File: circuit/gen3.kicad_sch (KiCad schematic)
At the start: 5 parts, among them J1 Conn_01x02_Socket, J2 Conn_02x20_Row_Letter_Last, J3 Conn_01x02_Socket, J4 Conn_02x20_Row_Letter_Last, U1 ESP32-DevKitC

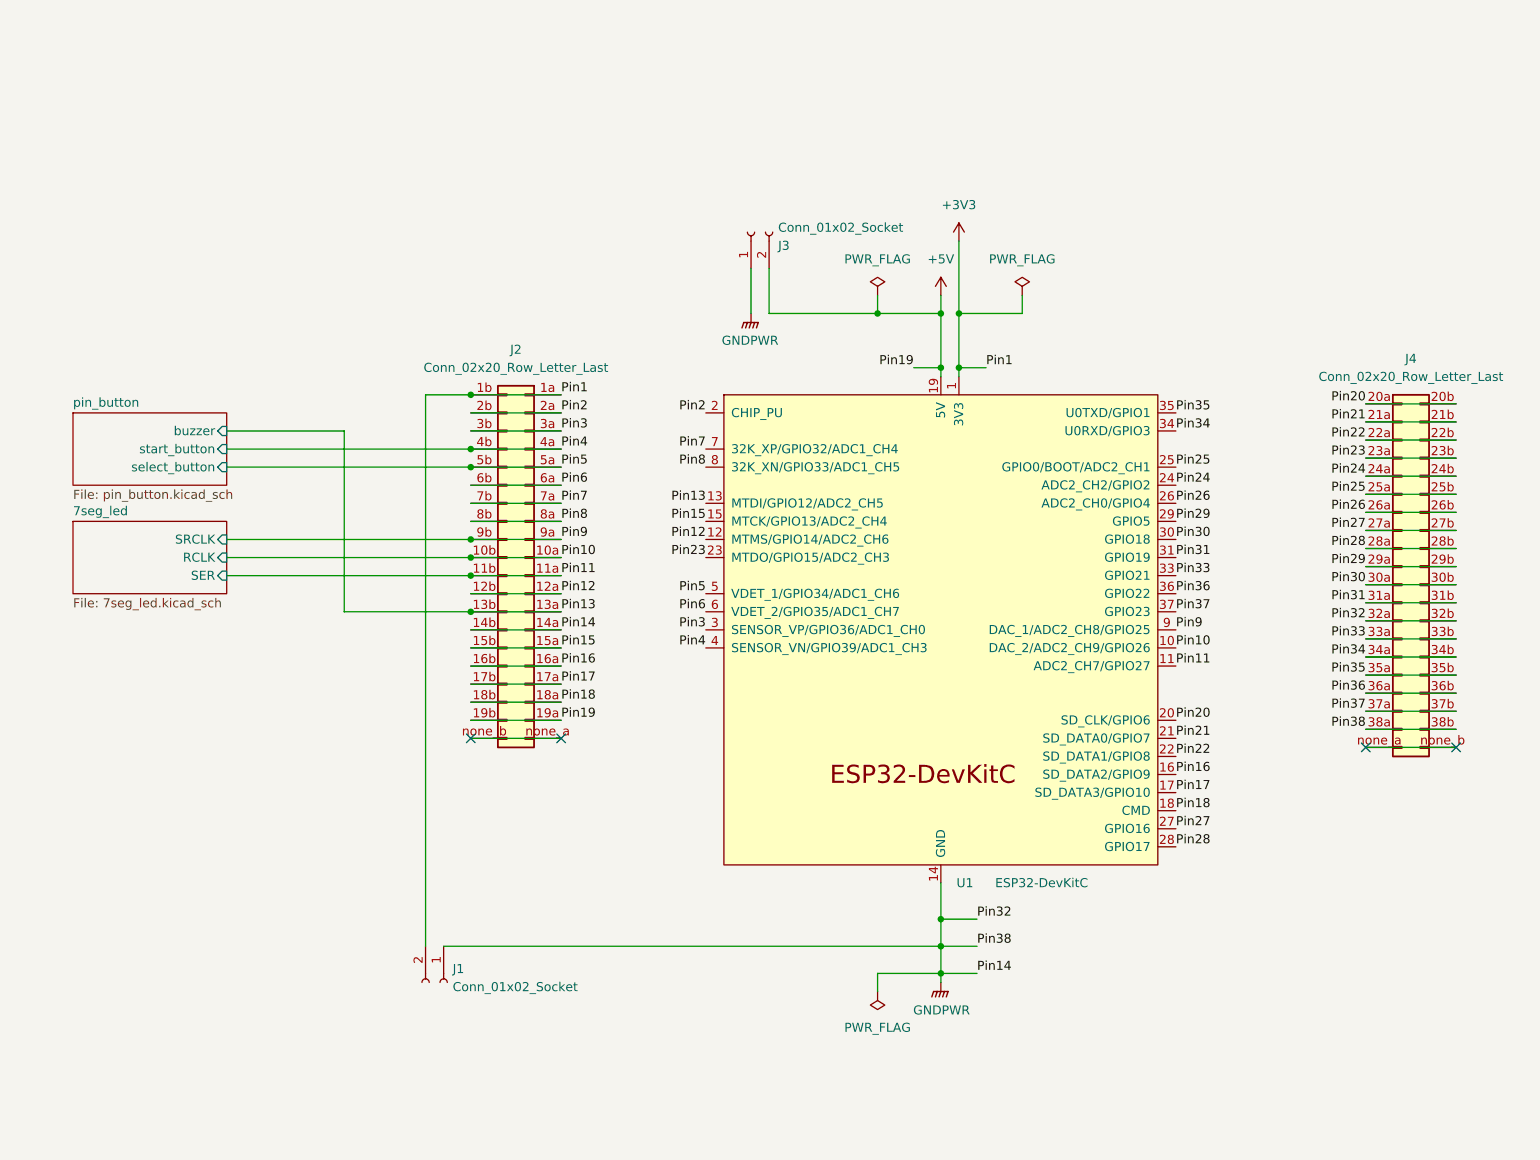
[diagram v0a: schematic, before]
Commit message: [add] add DC jack
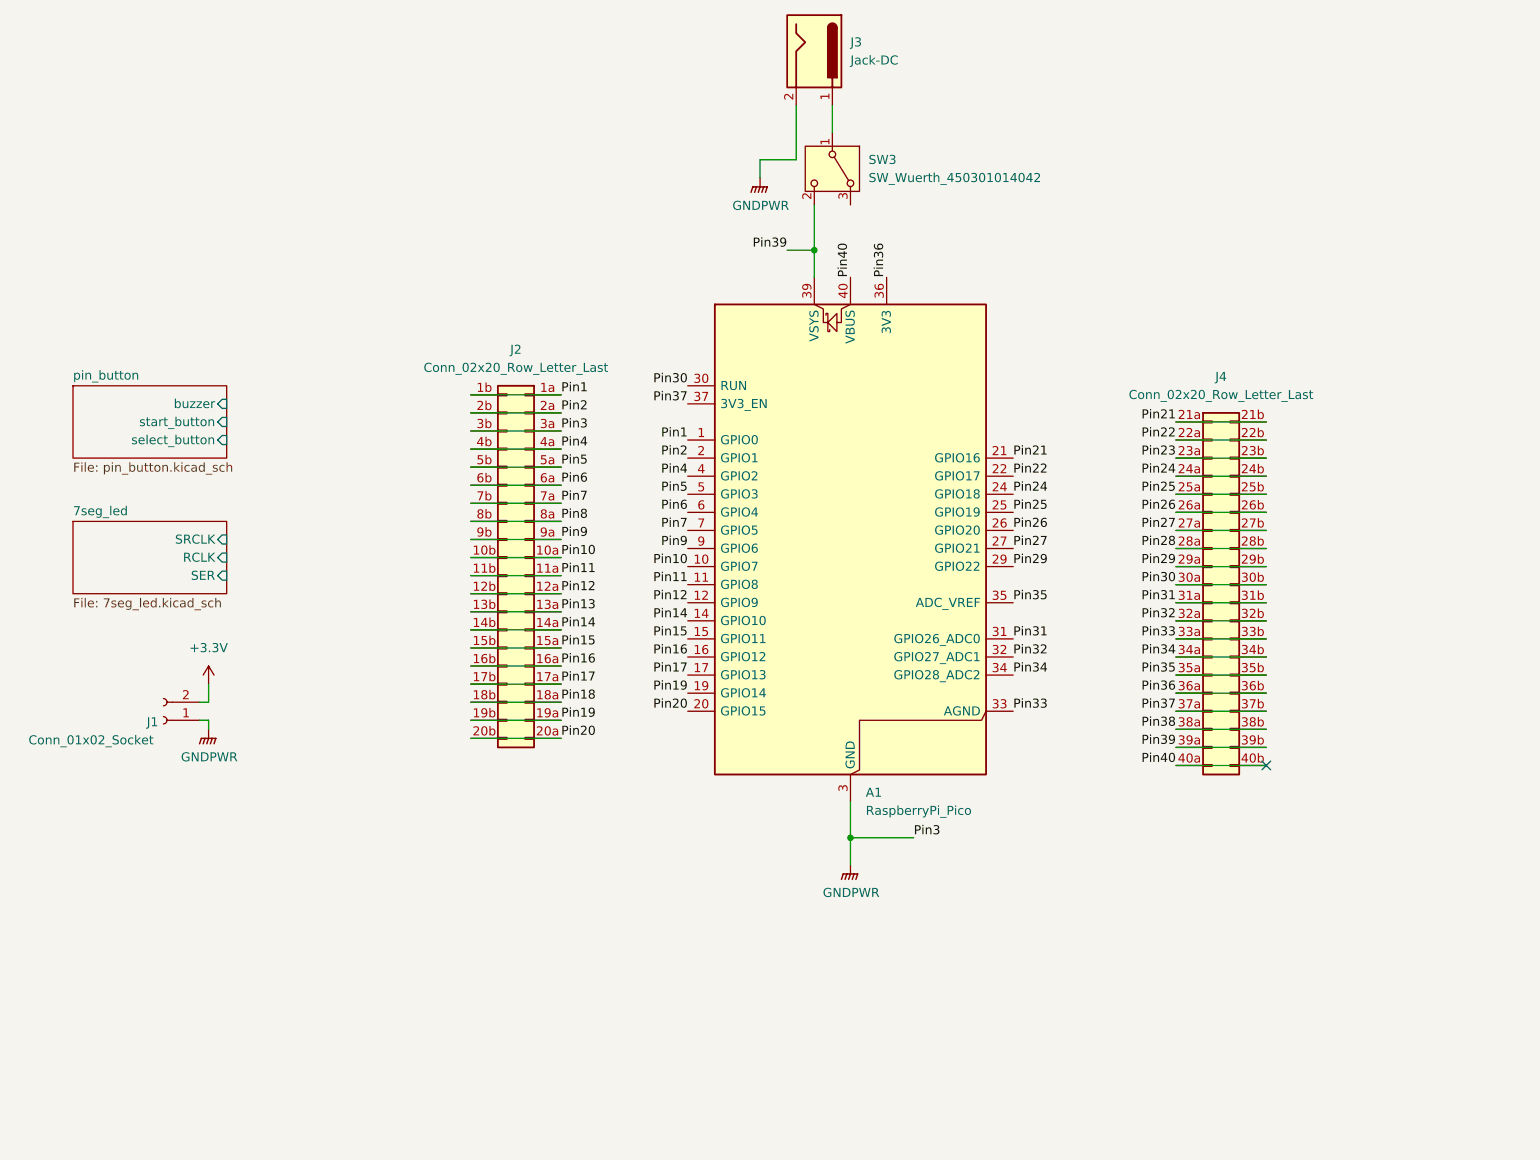
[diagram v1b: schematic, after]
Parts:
- removed J3: Conn_01x02_Socket, Connector_JST:JST_XH_S2B-XH-A_1x02_P2.50mm_Horizontal, symbol Connector:Conn_01x02_Socket
- removed U1: ESP32-DevKitC, MyPartsLibrary:ESP32-DevKitC, symbol PCM_Espressif:ESP32-DevKitC
- added A1: RaspberryPi_Pico, Module:RaspberryPi_Pico_Common_Unspecified, symbol MCU_Module:RaspberryPi_Pico
- added J3: Jack-DC, symbol Connector:Jack-DC
- added SW3: SW_Wuerth_450301014042, Button_Switch_THT:SW_Slide-03_Wuerth-WS-SLTV_10x2.5x6.4_P2.54mm, symbol Switch:SW_Wuerth_450301014042
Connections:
- net Pin3 is gone; now on net GNDPWR: J2.3a (Pin_3a), J2.3b (Pin_3b)
- net GNDPWR: now also A1.13 (GND), A1.18 (GND), A1.23 (GND), A1.28 (GND), A1.3 (GND), A1.38 (GND), A1.8 (GND), J3.2; no longer J2.14a (Pin_14a), J2.14b (Pin_14b), J4.32a (Pin_32a), J4.32b (Pin_32b), J4.38a (Pin_38a), J4.38b (Pin_38b)
- net Pin10: now also A1.10 (GPIO7)
- net Pin11: now also A1.11 (GPIO8)
- net Pin12: now also A1.12 (GPIO9)
- net Pin15: now also A1.15 (GPIO11)
- net Pin16: now also A1.16 (GPIO12)
- net Pin17: now also A1.17 (GPIO13)
- net Pin2: now also A1.2 (GPIO1)
- net Pin20: now also J2.20a (Pin_none_a), J2.20b (Pin_none_b), A1.20 (GPIO15); no longer J4.20a (Pin_20a), J4.20b (Pin_20b)
- net Pin21: now also A1.21 (GPIO16)
- net Pin22: now also A1.22 (GPIO17)
- net Pin24: now also A1.24 (GPIO18)
- net Pin25: now also A1.25 (GPIO19)
- net Pin26: now also A1.26 (GPIO20)
- net Pin27: now also A1.27 (GPIO21)
- net Pin29: now also A1.29 (GPIO22)
- net Pin30: now also A1.30 (RUN)
- net Pin31: now also A1.31 (GPIO26_ADC0)
- net Pin33: now also A1.33 (AGND)
- net Pin34: now also A1.34 (GPIO28_ADC2)
- net Pin35: now also A1.35 (ADC_VREF)
- net Pin36: now also A1.36 (3V3)
- net Pin37: now also A1.37 (3V3_EN)
- net Pin4: now also A1.4 (GPIO2)
- net Pin5: now also A1.5 (GPIO3)
- net Pin6: now also A1.6 (GPIO4)
- net Pin7: now also A1.7 (GPIO5)
- net Pin9: now also A1.9 (GPIO6)
- net +3V3 renamed Pin1
- net Pin1: now also A1.1 (GPIO0); no longer J1.2 (Pin_2)
- net +5V renamed Pin19
- net Pin19: now also A1.19 (GPIO14)
- new net: J3.1, SW3.1 (B)
- new net +3.3V: J1.2 (Pin_2)
- new net Pin14: A1.14 (GPIO10), J2.14a (Pin_14a), J2.14b (Pin_14b)
- new net Pin32: A1.32 (GPIO27_ADC1), J4.32a (Pin_32a), J4.32b (Pin_32b)
- new net Pin38: J4.38a (Pin_38a), J4.38b (Pin_38b)
- new net Pin39: A1.39 (VSYS), J4.39a (Pin_39a), J4.39b (Pin_39b), SW3.2 (C)
- new net Pin40: A1.40 (VBUS), J4.40a (Pin_40a), J4.40b (Pin_40b)
- no-connect marks 4 -> 1
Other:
- moved on the sheet: J1, J4

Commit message: [update] re-annotate symbols
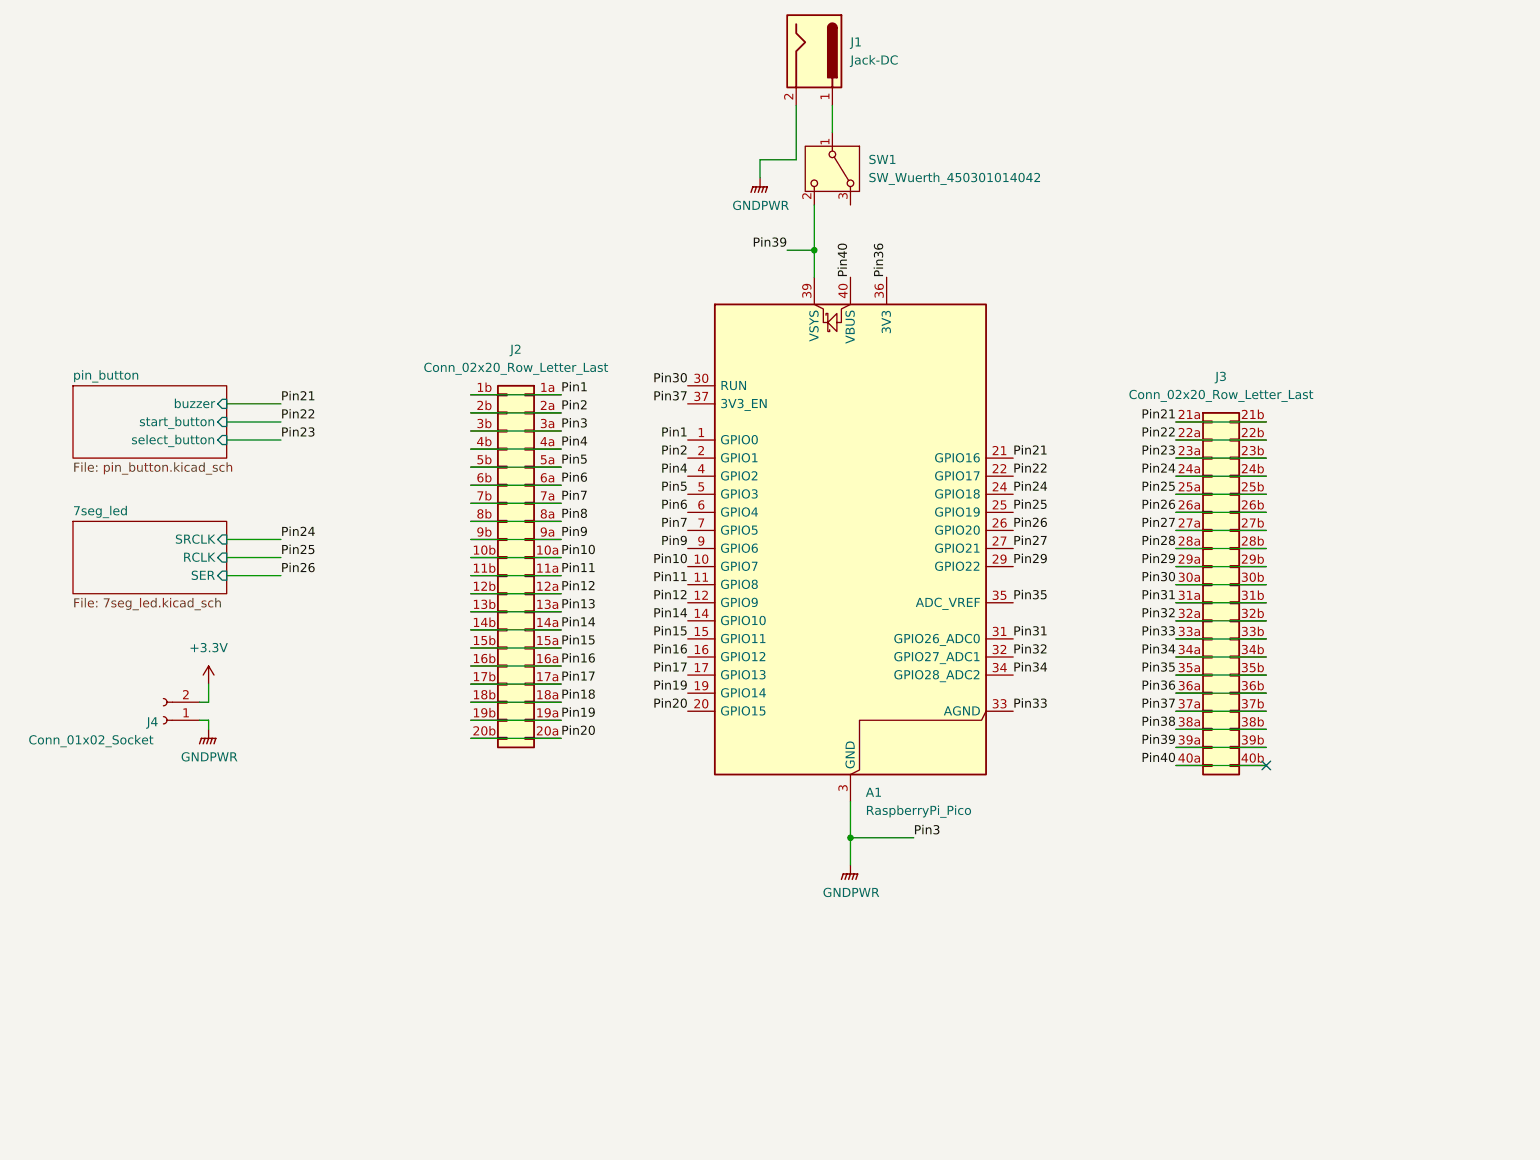
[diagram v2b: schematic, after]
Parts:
- renumbered J3 to J1, J4 to J3, J1 to J4, SW3 to SW1
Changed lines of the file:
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@@
+	(wire
+		(pts
+			(xy 76.2 72.39) (xy 83.82 72.39)
+		)
+		(stroke
+			(width 0)
+			(type default)
+		)
+	)
 	(wire
 		(pts
@@
 	(wire
 		(pts
+			(xy 76.2 93.98) (xy 83.82 93.98)
+		)
+		(stroke
+			(width 0)
+			(type default)
+		)
+	)
+	(wire
+		(pts
 			(xy 209.55 74.93) (xy 222.25 74.93)
 		)
@@
 	(wire
 		(pts
+			(xy 76.2 91.44) (xy 83.82 91.44)
+		)
+		(stroke
+			(width 0)
+			(type default)
+		)
+	)
+	(wire
+		(pts
+			(xy 76.2 77.47) (xy 83.82 77.47)
+		)
+		(stroke
+			(width 0)
+			(type default)
+		)
+	)
+	(wire
+		(pts
+			(xy 76.2 96.52) (xy 83.82 96.52)
+		)
+		(stroke
+			(width 0)
+			(type default)
+		)
+	)
+	(wire
+		(pts
 			(xy 110.49 91.44) (xy 123.19 91.44)
 		)
@@
 		(pts
 			(xy 151.13 38.1) (xy 156.21 38.1)
+		)
+		(stroke
+			(width 0)
+			(type default)
+		)
+	)
+	(wire
+		(pts
+			(xy 76.2 74.93) (xy 83.82 74.93)
 		)
 		(stroke
@@
 		)
 	)
+	(label "Pin23"
+		(at 83.82 77.47 0)
+		(effects
+			(font
+				(size 1.27 1.27)
+			)
+			(justify left bottom)
+		)
+	)
 	(label "Pin15"
 		(at 123.19 106.68 0)
@@
 		)
 	)
+	(label "Pin24"
+		(at 83.82 91.44 0)
+		(effects
+			(font
+				(size 1.27 1.27)
+			)
+			(justify left bottom)
+		)
+	)
 	(label "Pin28"
 		(at 209.55 92.71 180)
@@
 		)
 	)
+	(label "Pin26"
+		(at 83.82 96.52 0)
+		(effects
+			(font
+				(size 1.27 1.27)
+			)
+			(justify left bottom)
+		)
+	)
 	(label "Pin24"
 		(at 186.69 85.09 0)
@@
 		)
 	)
+	(label "Pin25"
+		(at 83.82 93.98 0)
+		(effects
+			(font
+				(size 1.27 1.27)
+			)
+			(justify left bottom)
+		)
+	)
 	(label "Pin2"
 		(at 123.19 73.66 0)
@@
 	(label "Pin1"
 		(at 123.19 71.12 0)
+		(effects
+			(font
+				(size 1.27 1.27)
+			)
+			(justify left bottom)
+		)
+	)
+	(label "Pin22"
+		(at 83.82 74.93 0)
+		(effects
+			(font
+				(size 1.27 1.27)
+			)
+			(justify left bottom)
+		)
+	)
+	(label "Pin21"
+		(at 83.82 72.39 0)
 		(effects
 			(font
@@
 		(on_board yes)
 		(dnp no)
-		(property "Reference" "#PWR020"
+		(property "Reference" "#PWR04"
 			(at 163.83 142.24 0)
 			(effects
@@
 			(project "gen3"
 				(path "/4fc99a72-ed0b-4d28-88d8-569af68d8cfc"
-					(reference "#PWR020")
+					(reference "#PWR04")
 					(unit 1)
 				)
@@
 		(on_board yes)
 		(dnp no)
-		(property "Reference" "J4"
+		(property "Reference" "J3"
 			(at 215.9 68.58 0)
 			(effects
@@
 			(project "gen3"
 				(path "/4fc99a72-ed0b-4d28-88d8-569af68d8cfc"
-					(reference "J4")
+					(reference "J3")
 					(unit 1)
 				)
@@
 		(dnp no)
 		(fields_autoplaced yes)
-		(property "Reference" "#PWR022"
+		(property "Reference" "#PWR02"
 			(at 73.66 115.57 0)
 			(effects
@@
 			(project ""
 				(path "/4fc99a72-ed0b-4d28-88d8-569af68d8cfc"
-					(reference "#PWR022")
+					(reference "#PWR02")
 					(unit 1)
 				)
@@
 		(on_board yes)
 		(dnp no)
-		(property "Reference" "#PWR023"
+		(property "Reference" "#PWR01"
 			(at 151.13 45.72 0)
 			(effects
@@
 			(project "gen3"
 				(path "/4fc99a72-ed0b-4d28-88d8-569af68d8cfc"
-					(reference "#PWR023")
+					(reference "#PWR01")
 					(unit 1)
 				)
@@
 		(dnp no)
 		(fields_autoplaced yes)
-		(property "Reference" "J3"
+		(property "Reference" "J1"
 			(at 163.83 21.5899 90)
 			(effects
@@
 			(project ""
 				(path "/4fc99a72-ed0b-4d28-88d8-569af68d8cfc"
-					(reference "J3")
+					(reference "J1")
 					(unit 1)
 				)
@@
 		(on_board yes)
 		(dnp no)
-		(property "Reference" "#PWR021"
+		(property "Reference" "#PWR03"
 			(at 73.66 123.19 0)
 			(effects
@@
 			(project "gen3"
 				(path "/4fc99a72-ed0b-4d28-88d8-569af68d8cfc"
-					(reference "#PWR021")
+					(reference "#PWR03")
 					(unit 1)
 				)
@@
 		(on_board yes)
 		(dnp no)
-		(property "Reference" "J1"
+		(property "Reference" "J4"
 			(at 65.786 117.094 0)
 			(effects
@@
 			(project "gen3"
 				(path "/4fc99a72-ed0b-4d28-88d8-569af68d8cfc"
-					(reference "J1")
+					(reference "J4")
 					(unit 1)
 				)
@@
 		(dnp no)
 		(fields_autoplaced yes)
-		(property "Reference" "SW3"
+		(property "Reference" "SW1"
 			(at 166.37 38.0999 90)
 			(effects
@@
 			(project ""
 				(path "/4fc99a72-ed0b-4d28-88d8-569af68d8cfc"
-					(reference "SW3")
+					(reference "SW1")
 					(unit 1)
 				)

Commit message: [wip][add] init pcb data
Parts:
- added H1, H2, H3, H4: MountingHole, symbol Mechanical:MountingHole
- A1: footprint Module:RaspberryPi_Pico_Common_Unspecified -> Module:RaspberryPi_Pico_Common_THT
- J1: footprint (none) -> Connector_BarrelJack:BarrelJack_Horizontal
- J2: footprint MyPartsLibrary:PinSocket_2x20_P2.54mm_1a-19a -> MyParts:PinSocket_2x20_P2.54mm_1a-20a
- J3: footprint MyPartsLibrary:PinSocket_2x20_P2.54mm_20a_38a -> MyParts:PinSocket_2x20_P2.54mm_20a_40a
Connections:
- net +3.3V is gone; now on net Pin36: J4.2 (Pin_2)
